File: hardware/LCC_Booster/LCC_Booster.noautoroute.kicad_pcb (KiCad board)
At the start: 2 copper layers, 150 x 100 mm, 88 parts, among them J1 A00-216-262-450, J2 Barrel_Jack_MountingPin, J3 Screw_Terminal_01x08, J4 Screw_Terminal_01x02, J5 Screw_Terminal_01x02, Q1 AO3400A, Q2 AO3400A, Q3 AO3400A, Q4 AO3400A, SW1 SW_Push, SW2 SW_Slide_DPDT, U1 ACPL-214-500E, U10 7410, U11 DRV8874PWPR, U12 7410, U13 7410, U14 7410, U15 7410, U16 DRV8874PWPR, U17 7410, U18 7410, U19 7410, U2 7410, U20 7410, U21 DRV8874PWPR, U22 MCP2515-xSO, U23 MCP2562-E-SN, U3 7410, U4 7410, U5 7410, U6 DRV8874PWPR, U7 7410, U8 7410, U9 7410, Y1 16.0 MHz, 22pF

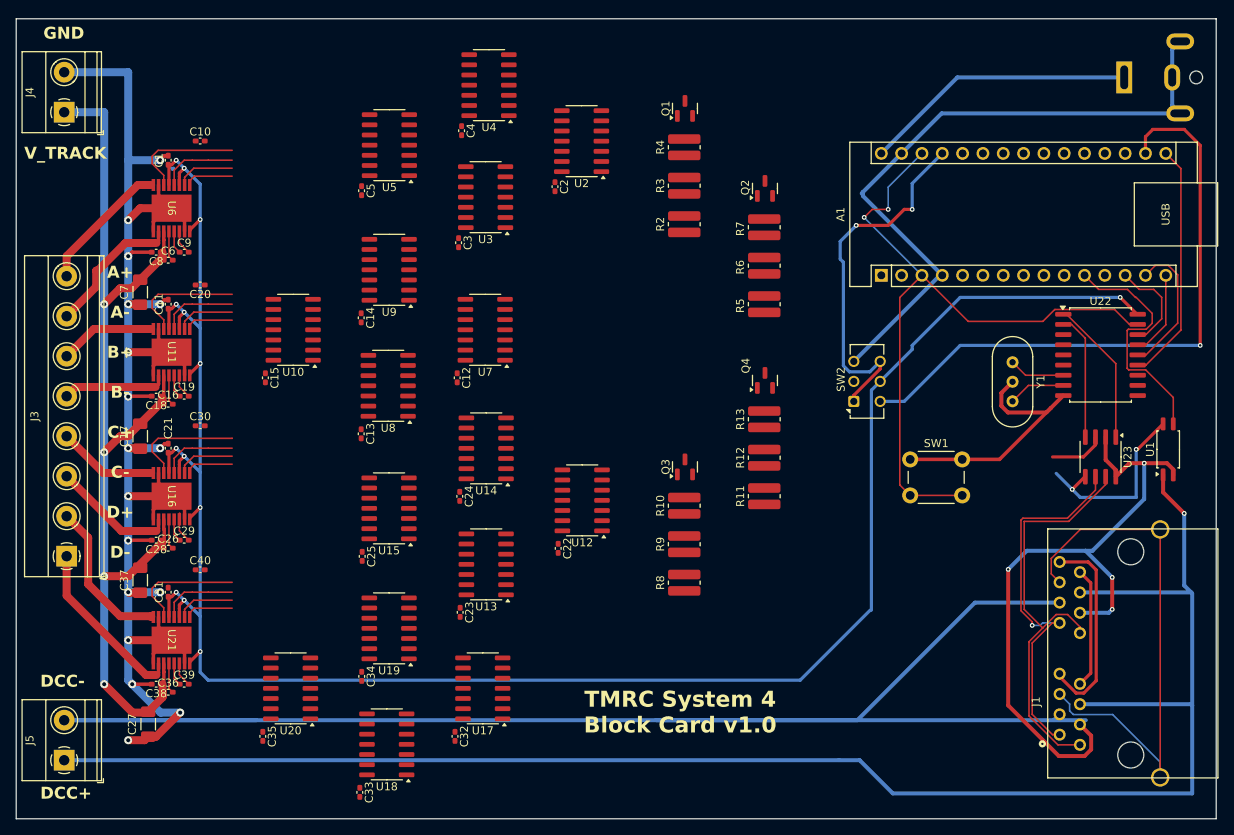
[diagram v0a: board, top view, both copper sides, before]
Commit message: Shrunk and added standoffs
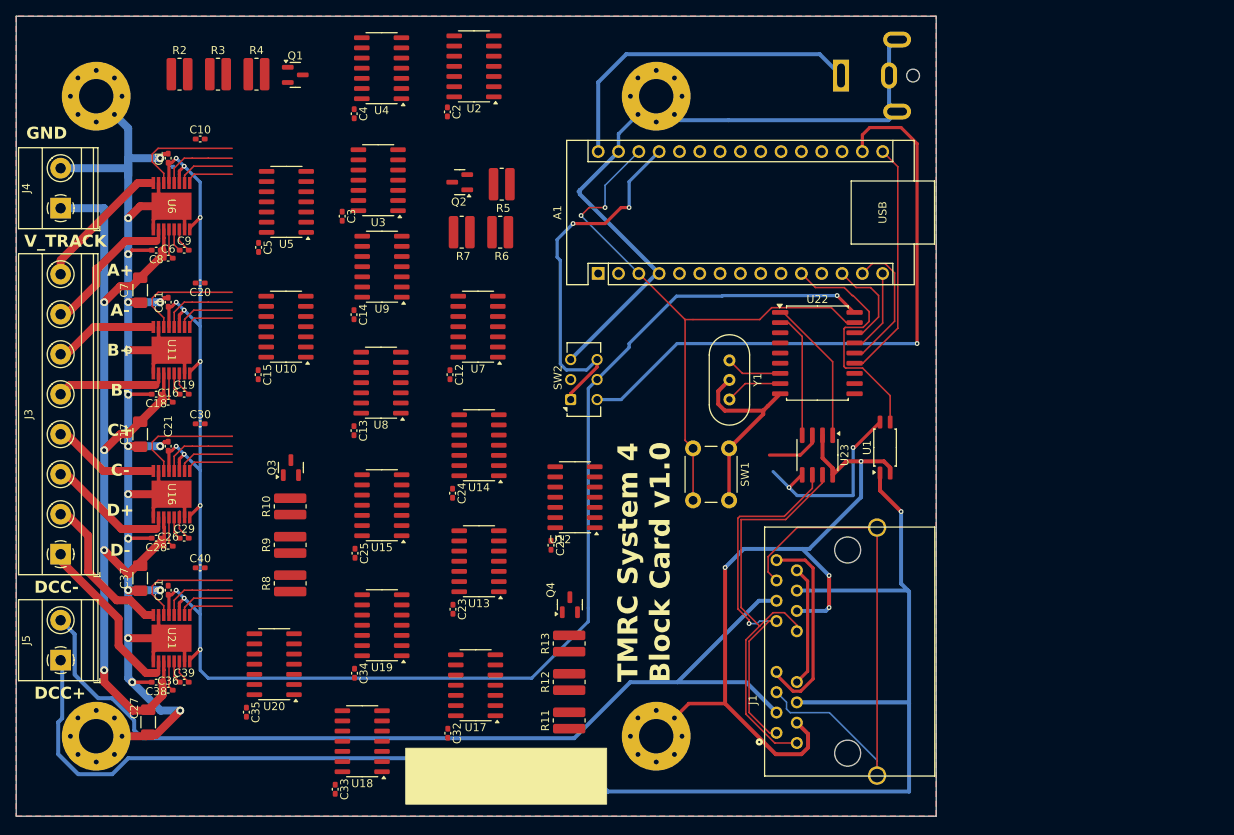
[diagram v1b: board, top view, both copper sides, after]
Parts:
- added H1: MountingHole_Pad, MountingHole:MountingHole_4.3mm_M4_Pad_Via, F.Cu at (30.0, 30.0)
- added H2: MountingHole_Pad, MountingHole:MountingHole_4.3mm_M4_Pad_Via, F.Cu at (30.0, 110.0)
- added H3: MountingHole_Pad, MountingHole:MountingHole_4.3mm_M4_Pad_Via, F.Cu at (100.0, 110.0)
- added H4: MountingHole_Pad, MountingHole:MountingHole_4.3mm_M4_Pad_Via, F.Cu at (100.0, 30.0)
- moved R2 65.8 mm to (40.4, 27.2), turned to 0 degrees
- moved R3 59.9 mm to (45.2, 27.2), turned to 0 degrees
- moved R4 54.2 mm to (50.0, 27.2), turned to 0 degrees
- moved Q3 49.3 mm to (54.3, 76.4)
- moved R10 49.3 mm to (54.2, 81.3)
- moved R8 49.3 mm to (54.2, 90.9)
- moved R9 49.3 mm to (54.2, 86.1)
- moved Q1 48.9 mm to (54.9, 27.3), turned to 0 degrees
- moved Q2 38.2 mm to (75.4, 40.8), turned to 180 degrees
- moved R7 37.8 mm to (75.7, 47.0), turned to 180 degrees
- moved Q4 37.2 mm to (89.2, 93.6)
- moved R11 37.2 mm to (89.1, 108.0)
- moved R12 37.2 mm to (89.1, 103.2)
- moved R13 37.2 mm to (89.1, 98.4)
- moved R5 36.1 mm to (80.7, 41.0), turned to 180 degrees
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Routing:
- net /raw_dcc_n: track 209.3 -> 120.3 mm
- net IOREF: track 289.3 -> 255.0 mm
- net GND: track 406.5 -> 421.1 mm, vias 21 -> 20
- net /~{reset}: track 88.9 -> 76.2 mm
- net /raw_dcc_p: track 212.0 -> 199.5 mm
- net VTRACK: track 133.0 -> 122.4 mm
- net VIN: track 34.3 -> 41.6 mm
- net /out1_D: track 19.2 -> 18.4 mm
- net /out2_B: track 13.2 -> 13.9 mm
- net /out1_C: track 12.5 -> 13.2 mm
- net /out1_B: track 12.0 -> 12.7 mm
- net /out2_A: track 17.7 -> 18.5 mm
- added copper zone on B.Cu, net GND
- added copper zone on F.Cu, net GND
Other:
- board size 150 x 100 mm -> 115 x 100 mm
